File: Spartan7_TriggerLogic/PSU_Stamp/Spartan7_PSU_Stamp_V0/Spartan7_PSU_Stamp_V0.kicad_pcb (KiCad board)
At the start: 4 copper layers, 24 x 32.5 mm, 53 parts, among them J1 USB4125-GF-A, J2 Castellated_holes, U1 LT3081EDF-TRPBF, U2 LT3081EDF-TRPBF, U3 TPS7A8801RTJT, U4 TPS7A8801RTJT, U5 TPS7A2033

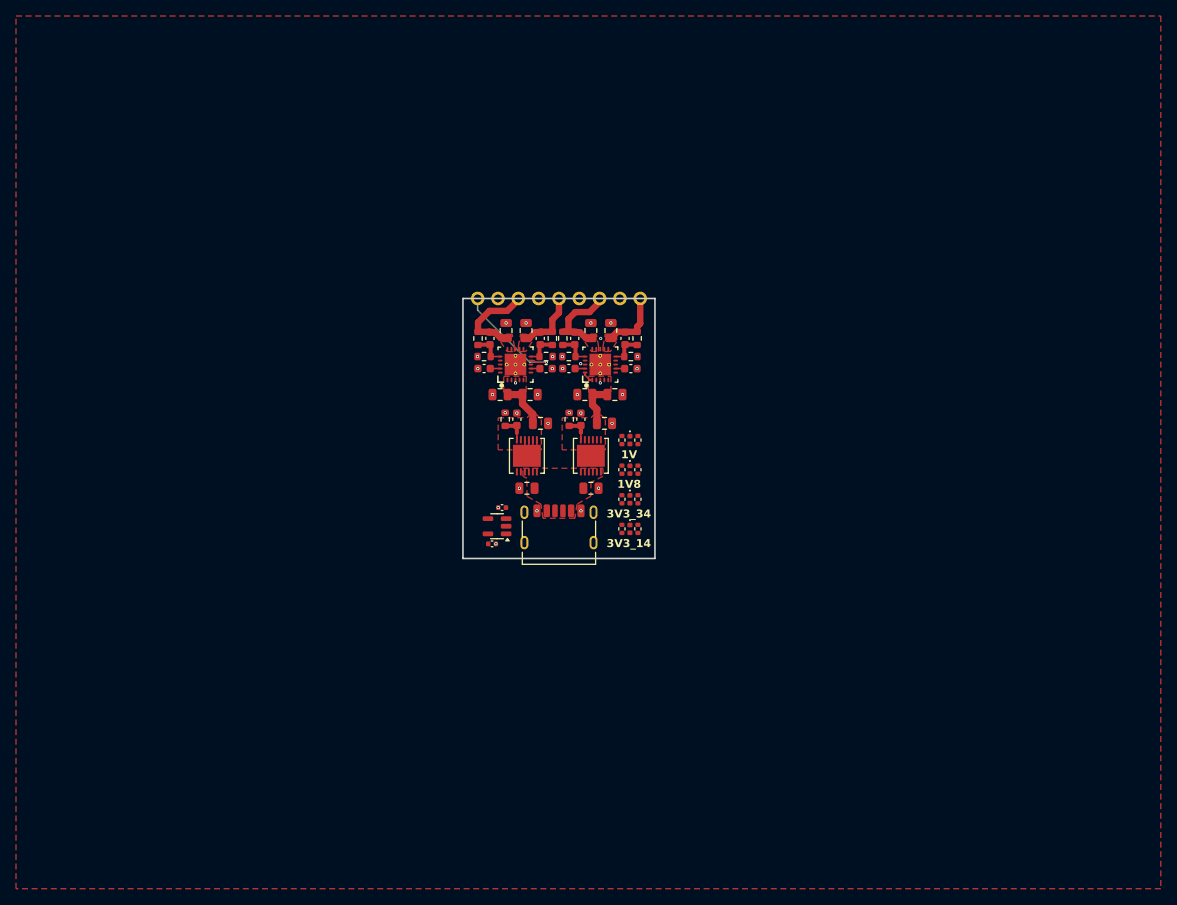
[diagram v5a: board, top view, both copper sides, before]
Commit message: Update PCB netlist and add GND test point
Renumbered and cleaned up net assignments in the KiCad PCB file, updated several resistor values, and added a new GND test point (J4). Also updated backup and plot files to reflect the latest schematic and layout changes.
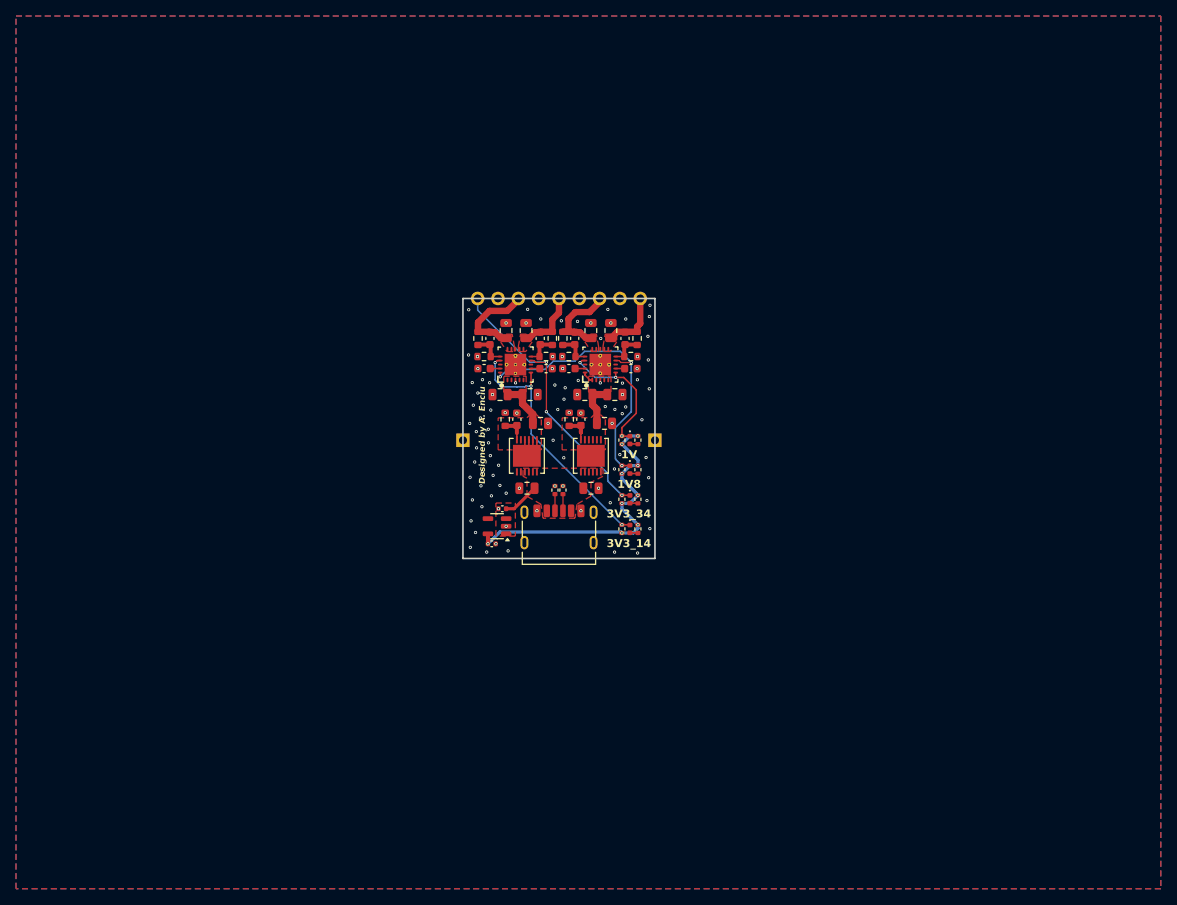
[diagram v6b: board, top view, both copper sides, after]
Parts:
- added J3: Conn_01x01_Pin, Connector_PinHeader_2.54mm:PinHeader_1x01_P2.54mm_Vertical, F.Cu at (148.1, 97.7)
- added J4: Conn_01x01_Pin, Connector_PinHeader_2.54mm:PinHeader_1x01_P2.54mm_Vertical, F.Cu at (124.1, 97.7)
- added R19: 5k1, Resistor_SMD:R_0402_1005Metric, F.Cu at (136.6, 104.0)
- added R20: 5k1, Resistor_SMD:R_0402_1005Metric, F.Cu at (135.6, 104.0)
- R10, R8: value R -> R_2
- R3, R4: value R -> R_3
- R5, R6: value R -> R_4
- R7, R9: value R -> R_1
- moved C23 0.14 mm to (129.0, 106.3)
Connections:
- J1 pad A5: unconnected-(J1-CC1-PadA5) -> Net-(J1-CC1)
- J1 pad B5: unconnected-(J1-CC2-PadB5) -> Net-(J1-CC2)
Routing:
- net +3V3: track 0.00 -> 39.1 mm, vias 0 -> 9
- net /PG_1V8_ok: track 0.00 -> 35.9 mm, vias 0 -> 3
- net /PG_3V3_14_ok: track 0.00 -> 32.6 mm, vias 0 -> 3
- net /DONE_0: track 14.8 -> 36.3 mm, vias 1 -> 3
- net /PG_1V_ok: track 0.00 -> 17.3 mm, vias 0 -> 3
- net +5V: track 0.00 -> 4.61 mm
- net Net-(J1-CC2): track 0.00 -> 2.08 mm
- net Net-(J1-CC1): track 0.00 -> 2.08 mm
- net Net-(D3-A): track 0.00 -> 1.01 mm
- net Net-(D2-A): track 0.00 -> 1.01 mm
- net Net-(D4-A): track 0.00 -> 1.01 mm
- net Net-(D1-A): track 0.00 -> 1.01 mm
- net GND: vias 32 -> 99
- added copper zone on B.Cu, net GND
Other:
- board text added: "Designed by A. Enciu"
- board text added: "PSU Stamp for Spartan7-FTGB196 REV_0, July 2025 TU Darmstadt"

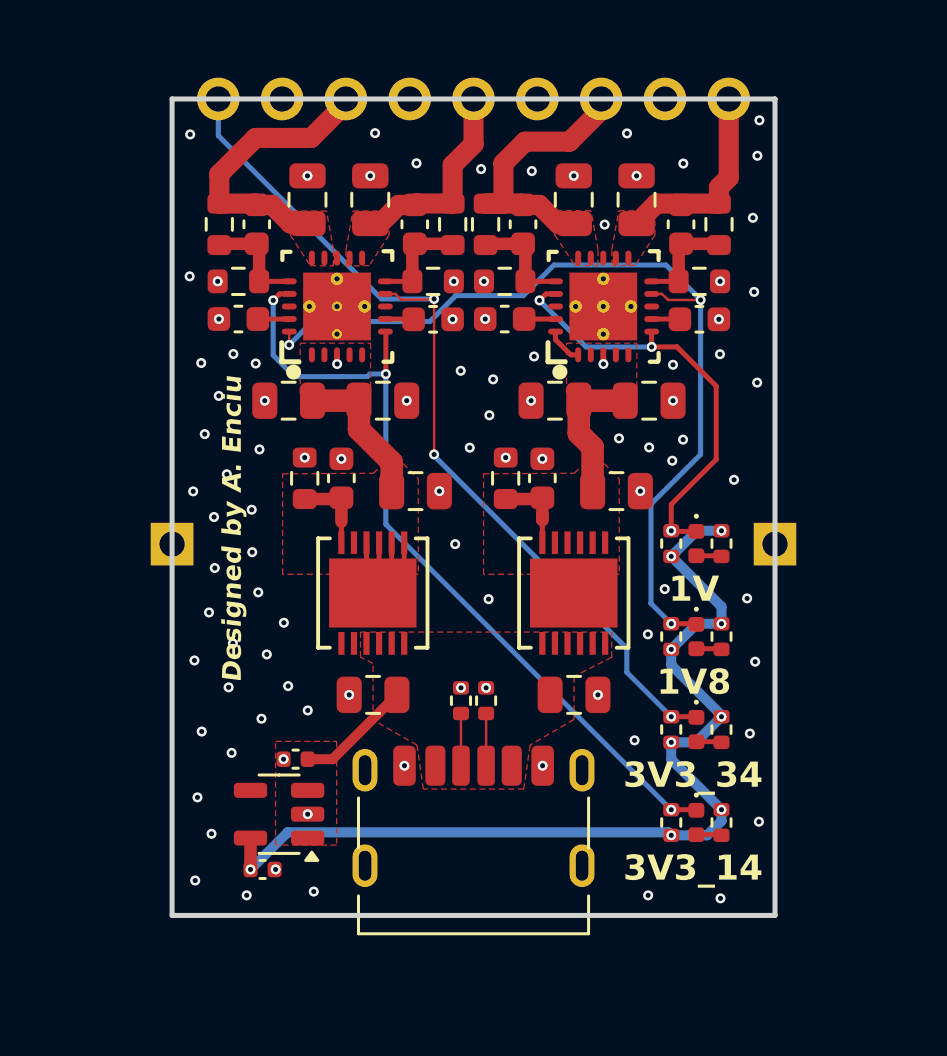
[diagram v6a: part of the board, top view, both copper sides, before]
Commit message: Add pin header footprints and update PCB layout
Replaced C14 footprint with a pin header (J10), added new pin headers J11 and J25, and updated the PCB layout parameters. Also swapped C13 and C14 positions and made related changes to the BOM and backup files.
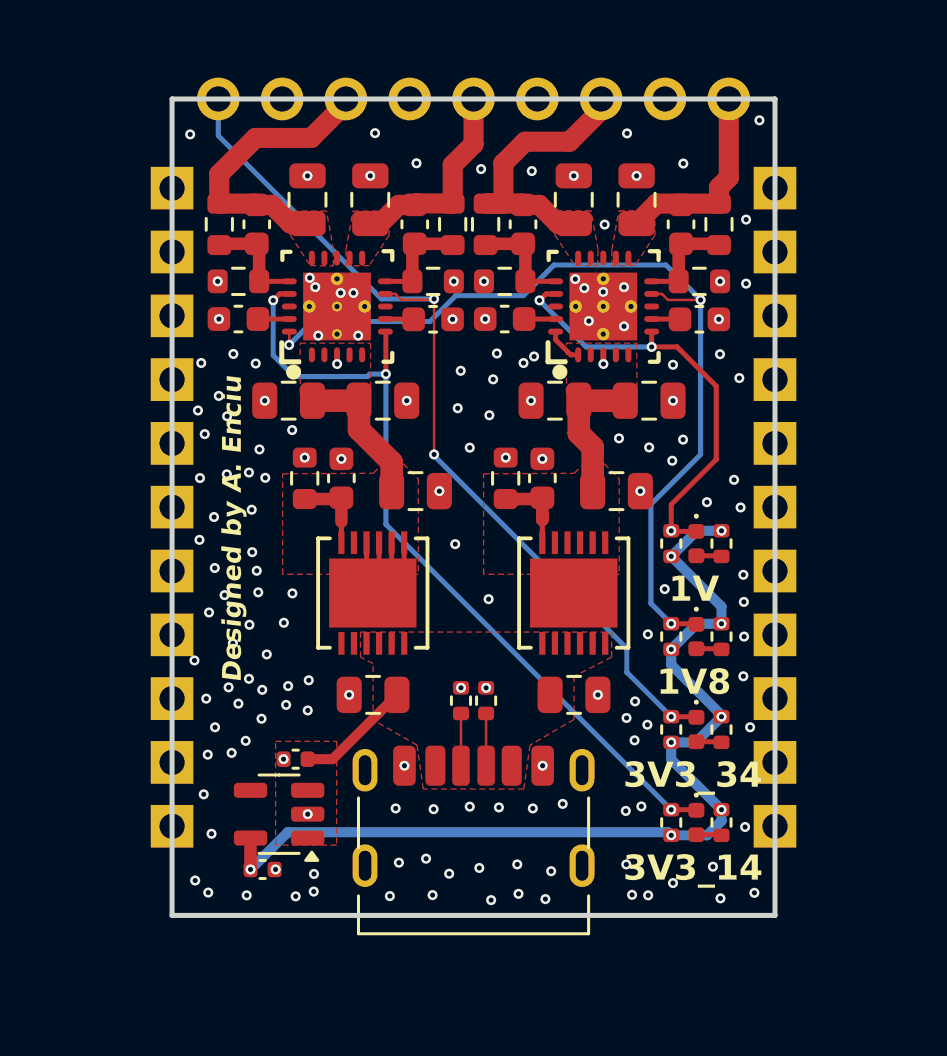
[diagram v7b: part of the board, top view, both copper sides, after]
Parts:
- removed J3, J4: Conn_01x01_Pin, Connector_PinHeader_2.54mm:PinHeader_1x01_P2.54mm_Vertical
- added J10: Conn_01x01_Pin, Connector_PinHeader_2.54mm:PinHeader_1x01_P2.54mm_Vertical, F.Cu at (124.1, 101.4)
- added J11: Conn_01x01_Pin, Connector_PinHeader_2.54mm:PinHeader_1x01_P2.54mm_Vertical, F.Cu at (148.1, 103.9)
- added J12: Conn_01x01_Pin, Connector_PinHeader_2.54mm:PinHeader_1x01_P2.54mm_Vertical, F.Cu at (124.1, 103.9)
- added J13: Conn_01x01_Pin, Connector_PinHeader_2.54mm:PinHeader_1x01_P2.54mm_Vertical, F.Cu at (148.1, 106.4)
- added J14: Conn_01x01_Pin, Connector_PinHeader_2.54mm:PinHeader_1x01_P2.54mm_Vertical, F.Cu at (124.1, 106.4)
- added J15: Conn_01x01_Pin, Connector_PinHeader_2.54mm:PinHeader_1x01_P2.54mm_Vertical, F.Cu at (148.1, 109.0)
- added J16: Conn_01x01_Pin, Connector_PinHeader_2.54mm:PinHeader_1x01_P2.54mm_Vertical, F.Cu at (124.1, 109.0)
- added J17: Conn_01x01_Pin, Connector_PinHeader_2.54mm:PinHeader_1x01_P2.54mm_Vertical, F.Cu at (148.1, 96.3)
- added J18: Conn_01x01_Pin, Connector_PinHeader_2.54mm:PinHeader_1x01_P2.54mm_Vertical, F.Cu at (124.1, 96.3)
- added J19: Conn_01x01_Pin, Connector_PinHeader_2.54mm:PinHeader_1x01_P2.54mm_Vertical, F.Cu at (148.1, 93.7)
- added J20: Conn_01x01_Pin, Connector_PinHeader_2.54mm:PinHeader_1x01_P2.54mm_Vertical, F.Cu at (124.1, 93.7)
- added J21: Conn_01x01_Pin, Connector_PinHeader_2.54mm:PinHeader_1x01_P2.54mm_Vertical, F.Cu at (148.1, 91.2)
- added J22: Conn_01x01_Pin, Connector_PinHeader_2.54mm:PinHeader_1x01_P2.54mm_Vertical, F.Cu at (124.1, 91.2)
- added J23: Conn_01x01_Pin, Connector_PinHeader_2.54mm:PinHeader_1x01_P2.54mm_Vertical, F.Cu at (148.1, 88.7)
- added J24: Conn_01x01_Pin, Connector_PinHeader_2.54mm:PinHeader_1x01_P2.54mm_Vertical, F.Cu at (124.1, 88.7)
- added J25: Conn_01x01_Pin, Connector_PinHeader_2.54mm:PinHeader_1x01_P2.54mm_Vertical, F.Cu at (148.1, 86.1)
- added J26: Conn_01x01_Pin, Connector_PinHeader_2.54mm:PinHeader_1x01_P2.54mm_Vertical, F.Cu at (124.1, 86.1)
- added J27: Conn_01x01_Pin, Connector_PinHeader_2.54mm:PinHeader_1x01_P2.54mm_Vertical, F.Cu at (148.1, 83.6)
- added J28: Conn_01x01_Pin, Connector_PinHeader_2.54mm:PinHeader_1x01_P2.54mm_Vertical, F.Cu at (124.1, 83.6)
- added J7: Conn_01x01_Pin, Connector_PinHeader_2.54mm:PinHeader_1x01_P2.54mm_Vertical, F.Cu at (148.1, 98.8)
- added J8: Conn_01x01_Pin, Connector_PinHeader_2.54mm:PinHeader_1x01_P2.54mm_Vertical, F.Cu at (124.1, 98.8)
- added J9: Conn_01x01_Pin, Connector_PinHeader_2.54mm:PinHeader_1x01_P2.54mm_Vertical, F.Cu at (148.1, 101.4)
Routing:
- net GND: vias 99 -> 164

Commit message: .
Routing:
- net +5V: track 4.61 -> 5.78 mm
- net /V_Bank_14_3V3: track 11.4 -> 11.9 mm
- net GND: vias 164 -> 175
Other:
- board text added: "34&14"
- board text added: "Bnk_0"
- board text removed: "3V3_14"
- board text removed: "3V3_34"
